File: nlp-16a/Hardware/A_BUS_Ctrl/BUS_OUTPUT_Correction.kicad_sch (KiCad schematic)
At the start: 21 parts, among them U44 CD74HC00

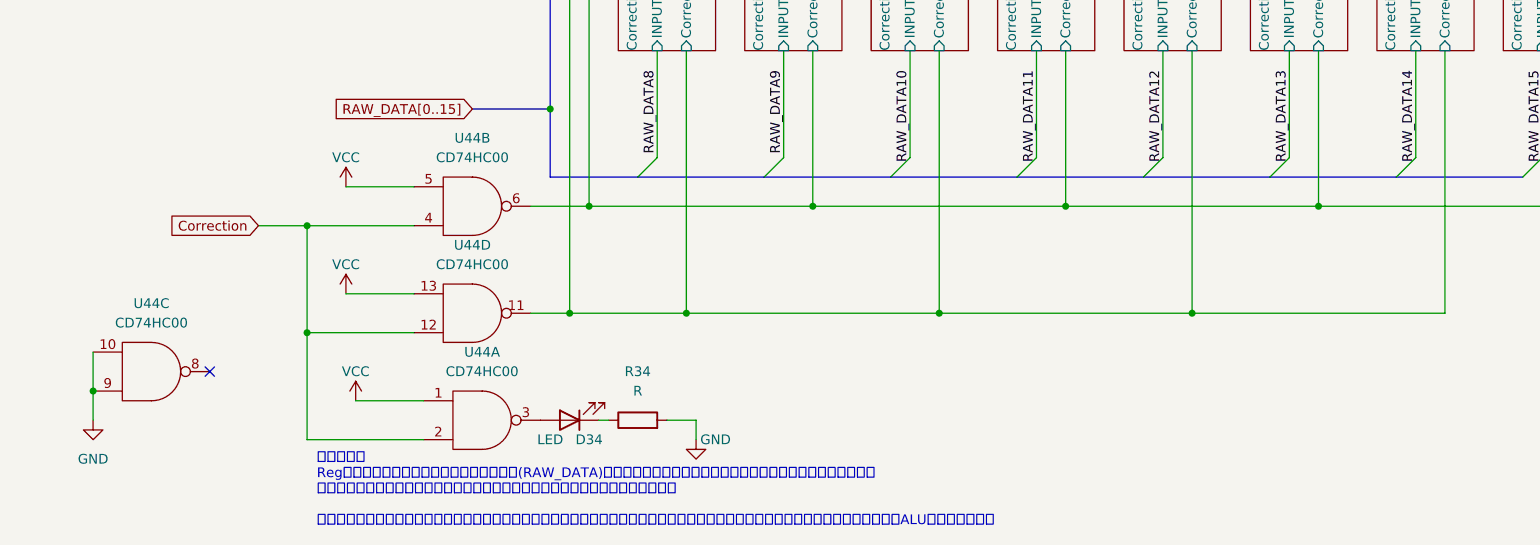
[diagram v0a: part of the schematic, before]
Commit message: テストで見つかった不具合を修正(れジスタアドレスデコーダ，Addrの内部処理の方法を変更)
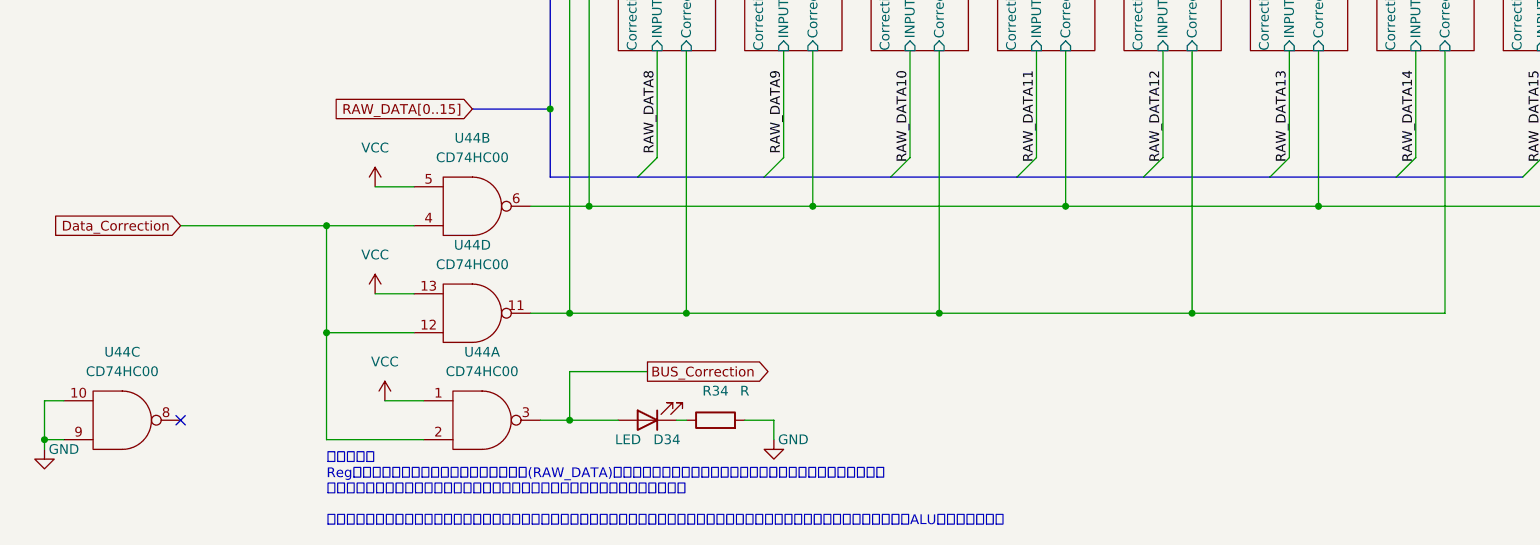
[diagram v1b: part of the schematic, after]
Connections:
- net BUS_Correction: now reaches D34.2 (A), U44.3
- net Correction renamed Data_Correction
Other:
- moved on the sheet: D34, R34, U44C
